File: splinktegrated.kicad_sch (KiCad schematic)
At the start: 126 parts, among them J1 USB_C_Receptacle_USB2.0, J10 NA_Ribbon, J13 Conn_01x01_Socket, J14 Cirque, J15 Conn_01x01_Socket, J16 Conn_01x01_Socket, J17 Conn_01x01_Socket, J18 USB_C_Receptacle_USB2.0, J19 Conn_01x01_Socket, J20 Conn_01x01_Socket, J5 Conn_01x02, J6 Cirque, J7 NA_trackball, J8 NA_Ribbon, J9 NA_RGB, Q4 AO3401A, Q5 AO3401A, SW2 NA_SW_SPST, SW9001 NA_SW_SPST, U1 RP2040, U2 USBLC6-2P6, U3 XC6210B332MR-G, U4 USBLC6-2P6, U5 W25Q128JVS, U6 74LVC1T45, Y1 Crystal_GND24

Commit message: connect stuff
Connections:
- net D+: no longer right_J9001.A6 (D+), right_J9001.B6 (D+), right_R9005.1, right_U9003.3 (I/O2), right_U9003.4 (I/O2)
- net D-: no longer right_J9001.A7 (D-), right_J9001.B7 (D-), right_R9006.1, right_U9003.1 (I/O1), right_U9003.6 (I/O1)
- net GND: no longer SW9001.2 (B), right_C9000.2, right_C9001.2, right_C9002.2, right_C9003.2, right_C9004.2, right_C9005.2, right_C9006.2, right_C9007.2, right_C9008.2, right_C9009.2, right_C9010.2, right_C9011.2, right_C9012.2, right_C9013.2, right_D9000.2 (A2), right_FB9001.1, right_FB9002.1, right_H9001.1, right_H9003.1, right_J9000.A1 (GND), right_J9000.A12 (GND), right_J9000.B1 (GND), right_J9000.B12 (GND), right_J9001.A1 (GND), right_J9001.A12 (GND), right_J9001.B1 (GND), right_J9001.B12 (GND), right_J9004.1 (Pin_1), right_J9006.2 (Pin_2), right_J9008.6 (Pin_6), right_J9014.11 (Pin_11), right_Q9000.1 (G), right_Q9001.1 (G), right_R9000.2, right_R9001.2, right_R9002.1, right_R9010.1, right_R9011.1, right_U9000.2 (GND), right_U9001.2 (GND), right_U9002.2 (GND), right_U9003.2 (GND), right_U9004.4 (GND), right_U9005.19 (TESTEN), right_U9005.57 (GND), right_Y9000.2, right_Y9000.4
- net rgb_5V: no longer right_J9006.3 (Pin_3), right_J9014.8 (Pin_8), right_U9001.4 (B)
- new net right_D+: right_J9001.A6 (D+), right_J9001.B6 (D+), right_R9005.1, right_U9003.3 (I/O2), right_U9003.4 (I/O2)
- new net right_D-: right_J9001.A7 (D-), right_J9001.B7 (D-), right_R9006.1, right_U9003.1 (I/O1), right_U9003.6 (I/O1)
- new net right_GND: SW9001.2 (B), right_C9000.2, right_C9001.2, right_C9002.2, right_C9003.2, right_C9004.2, right_C9005.2, right_C9006.2, right_C9007.2, right_C9008.2, right_C9009.2, right_C9010.2, right_C9011.2, right_C9012.2, right_C9013.2, right_D9000.2 (A2), right_FB9001.1, right_FB9002.1, right_H9001.1, right_H9003.1, right_J9000.A1 (GND), right_J9000.A12 (GND), right_J9000.B1 (GND), right_J9000.B12 (GND), right_J9001.A1 (GND), right_J9001.A12 (GND), right_J9001.B1 (GND), right_J9001.B12 (GND), right_J9004.1 (Pin_1), right_J9006.2 (Pin_2), right_J9008.6 (Pin_6), right_J9014.11 (Pin_11), right_Q9000.1 (G), right_Q9001.1 (G), right_R9000.2, right_R9001.2, right_R9002.1, right_R9010.1, right_R9011.1, right_U9000.2 (GND), right_U9001.2 (GND), right_U9002.2 (GND), right_U9003.2 (GND), right_U9004.4 (GND), right_U9005.19 (TESTEN), right_U9005.57 (GND), right_Y9000.2, right_Y9000.4
- new net right_rgb_5V: right_J9006.3 (Pin_3), right_J9014.8 (Pin_8), right_U9001.4 (B)
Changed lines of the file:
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@@
 		)
 	)
-	(text "Old"
-		(exclude_from_sim no)
-		(at -67.31 384.81 0)
-		(effects
-			(font
-				(size 1.778 1.778)
-				(thickness 0.3556)
-				(bold yes)
-			)
-			(justify left bottom)
-		)
-	)
 	(text "Indicator & buttons"
 		(exclude_from_sim no)
@@
 		)
 	)
-	(wire
-		(pts
-			(xy -53.34 391.16) (xy -44.45 391.16)
-		)
-		(stroke
-			(width 0)
-			(type default)
-		)
-	)
 	(polyline
 		(pts
@@
 	(wire
 		(pts
-			(xy -53.34 388.62) (xy -44.45 388.62)
-		)
-		(stroke
-			(width 0)
-			(type default)
-		)
-	)
-	(wire
-		(pts
 			(xy 287.02 370.84) (xy 275.59 370.84)
 		)
@@
 	(wire
 		(pts
-			(xy -53.34 396.24) (xy -44.45 396.24)
-		)
-		(stroke
-			(width 0)
-			(type default)
-		)
-	)
-	(wire
-		(pts
 			(xy 248.92 370.84) (xy 250.19 370.84)
 		)
@@
 		)
 	)
-	(wire
-		(pts
-			(xy -53.34 393.7) (xy -44.45 393.7)
-		)
-		(stroke
-			(width 0)
-			(type default)
-		)
-	)
 	(polyline
 		(pts
@@
 		)
 	)
-	(label "D-_daughter"
-		(at -53.34 393.7 180)
-		(effects
-			(font
-				(size 1.27 1.27)
-			)
-			(justify right bottom)
-		)
-	)
 	(label "right_SCLK"
 		(at 274.32 300.99 0)
@@
 		)
 	)
-	(label "Vbus_mother"
-		(at -44.45 388.62 0)
-		(effects
-			(font
-				(size 1.27 1.27)
-			)
-			(justify left bottom)
-		)
-	)
-	(label "right_D-"
-		(at -44.45 393.7 0)
-		(effects
-			(font
-				(size 1.27 1.27)
-			)
-			(justify left bottom)
-		)
-	)
 	(label "right_D0"
 		(at 210.82 299.72 180)
@@
 		)
 	)
-	(label "right_D+"
-		(at -44.45 396.24 0)
-		(effects
-			(font
-				(size 1.27 1.27)
-			)
-			(justify left bottom)
-		)
-	)
-	(label "D+_daughter"
-		(at -53.34 396.24 180)
-		(effects
-			(font
-				(size 1.27 1.27)
-			)
-			(justify right bottom)
-		)
-	)
 	(label "right_D14"
 		(at 322.58 335.28 0)
@@
 		)
 	)
-	(label "Vbus_daughter"
-		(at -53.34 388.62 180)
-		(effects
-			(font
-				(size 1.27 1.27)
-			)
-			(justify right bottom)
-		)
-	)
 	(label "right_SCLK"
 		(at 210.82 355.6 180)
@@
 		)
 	)
-	(label "Gnd_daughter"
-		(at -53.34 391.16 180)
-		(effects
-			(font
-				(size 1.27 1.27)
-			)
-			(justify right bottom)
-		)
-	)
 	(label "right_LED"
 		(at 210.82 342.9 180)
@@
 		)
 	)
-	(global_label "rgb_5V"
+	(global_label "right_rgb_5V"
 		(shape input)
 		(at 353.06 273.05 180)
@@
 		)
 	)
-	(global_label "rgb_5V"
+	(global_label "right_rgb_5V"
 		(shape input)
 		(at 450.85 285.75 180)
@@
 		)
 	)
-	(global_label "rgb_5V"
+	(global_label "right_rgb_5V"
 		(shape input)
 		(at 363.22 408.94 0)
@@
 					(unit 1)
 				)
-			)
-		)
-	)
-	(symbol
-		(lib_id "power:GND")
-		(at -44.45 391.16 90)
-		(unit 1)
-		(exclude_from_sim no)
-		(in_bom yes)
-		(on_board yes)
-		(dnp no)
-		(property "Reference" "#PWR058"
-			(at -38.1 391.16 0)
-			(effects
-				(font
-					(size 1.27 1.27)
-				)
-				(hide yes)
-			)
-		)
-		(property "Value" "right_GND"
-			(at -37.4651 391.316 90)
-			(effects
-				(font
-					(size 1.27 1.27)
-				)
-				(justify left)
-			)
-		)
-		(property "Footprint" ""
-			(at -44.45 391.16 0)
-			(effects
-				(font
-					(size 1.27 1.27)
-				)
-				(hide yes)
-			)
-		)
-		(property "Datasheet" ""
-			(at -44.45 391.16 0)
-			(effects
-				(font
-					(size 1.27 1.27)
-				)
-				(hide yes)
-			)
-		)
-		(property "Description" ""
-			(at -44.45 391.16 0)
-			(effects
-				(font
-					(size 1.27 1.27)
-				)
-				(hide yes)
-			)
-		)
-		(pin "1"
-		)
-		(instances
-			(project "splinktegrated"
-				(path "/7353e96a-343a-4876-b497-b1d205a14d97"
-					(reference "#PWR058")
-					(unit 1)
-				)

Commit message: change push button
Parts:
- J5, right_J9004: footprint drawings:PinHeader_1x02_P1.27mm_Vertical -> Button_Switch_SMD:SW_SPST_CK_KXT3
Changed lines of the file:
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@@
 			)
 		)
-		(property "Footprint" "drawings:PinHeader_1x02_P1.27mm_Vertical"
+		(property "Footprint" "Button_Switch_SMD:SW_SPST_CK_KXT3"
 			(at 69.215 174.625 0)
 			(effects
@@
 			)
 		)
-		(property "Footprint" "drawings:PinHeader_1x02_P1.27mm_Vertical"
+		(property "Footprint" "Button_Switch_SMD:SW_SPST_CK_KXT3"
 			(at 88.265 415.925 0)
 			(effects

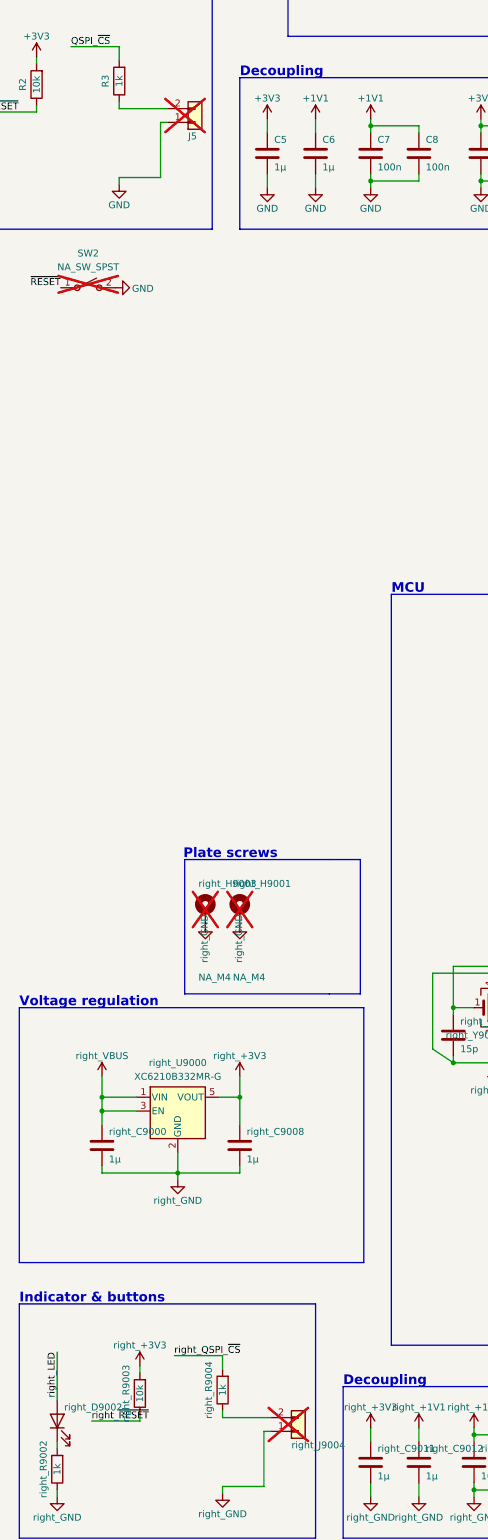
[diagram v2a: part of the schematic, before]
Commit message: populate hardware fallback button
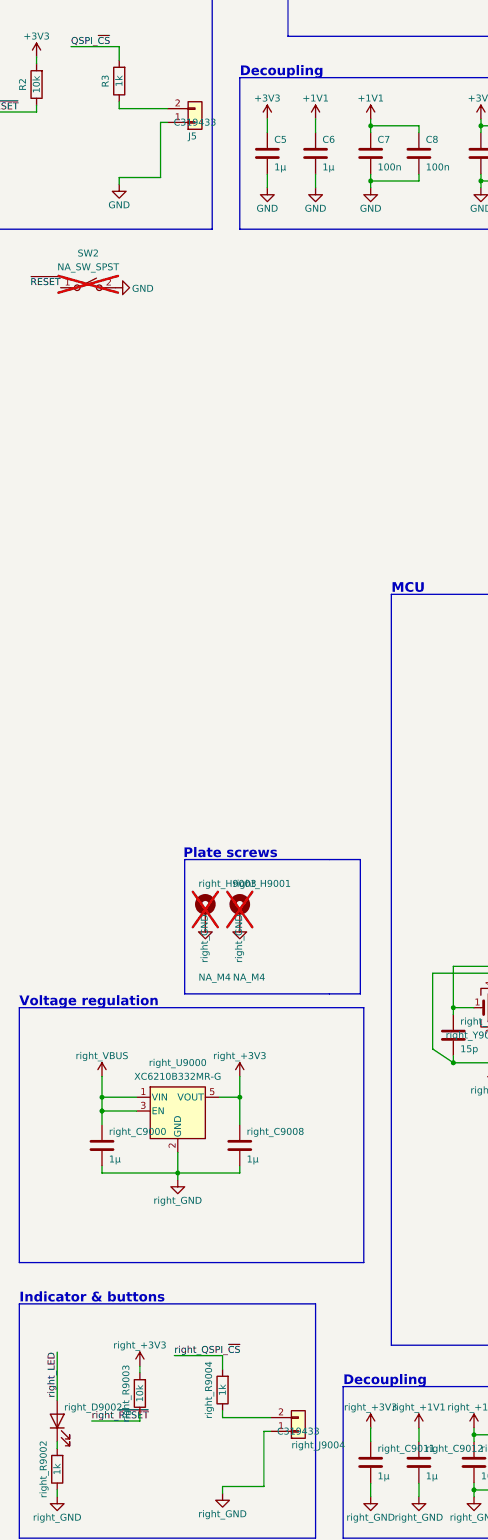
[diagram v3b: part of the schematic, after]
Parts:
- J5, right_J9004: LCSC (none) -> C319433; now fitted; now in the parts list
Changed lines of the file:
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@@
 		(unit 1)
 		(exclude_from_sim no)
-		(in_bom no)
+		(in_bom yes)
 		(on_board yes)
-		(dnp yes)
+		(dnp no)
 		(property "Reference" "J5"
 			(at 67.945 177.165 0)
@@
 			)
 		)
+		(property "LCSC" "C319433"
+			(at 69.215 174.625 0)
+			(effects
+				(font
+					(size 1.27 1.27)
+				)
+			)
+		)
 		(pin "1"
 		)
@@
 		(unit 1)
 		(exclude_from_sim no)
-		(in_bom no)
+		(in_bom yes)
 		(on_board yes)
-		(dnp yes)
+		(dnp no)
 		(property "Reference" "right_J9004"
 			(at 86.995 418.465 0)
@@
 			)
 		)
+		(property "LCSC" "C319433"
+			(at 88.265 415.925 0)
+			(effects
+				(font
+					(size 1.27 1.27)
+				)
+			)
+		)

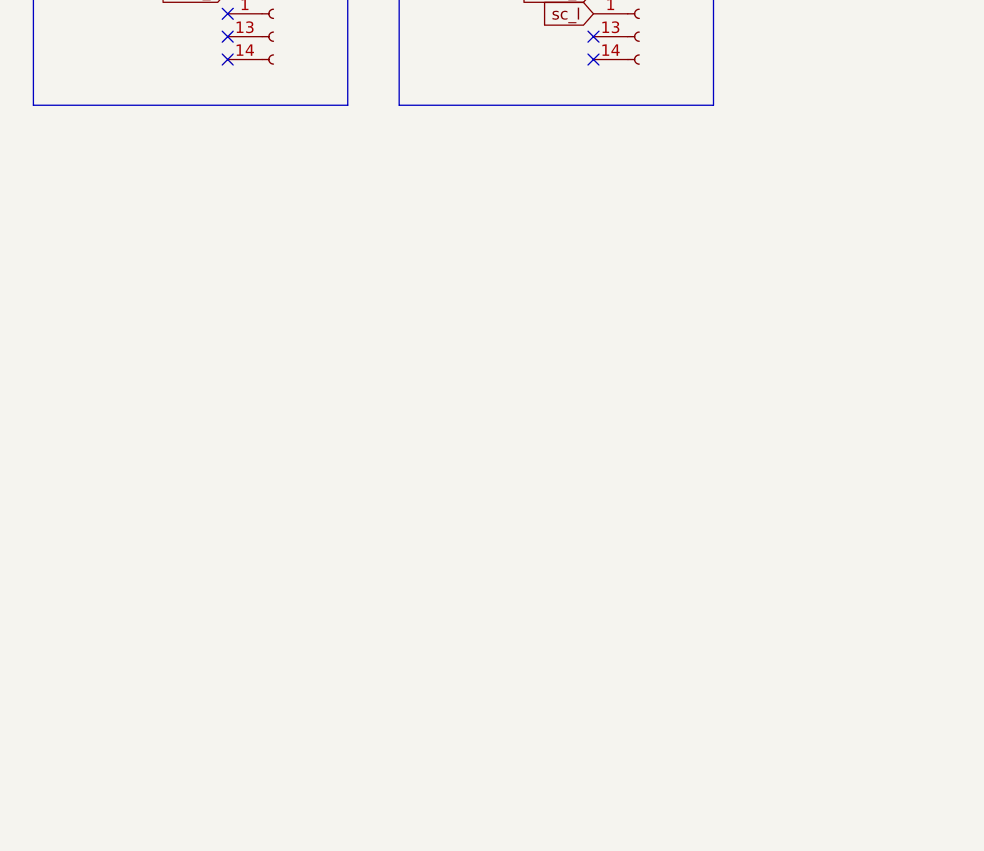
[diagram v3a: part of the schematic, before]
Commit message: add tvs diodes... so many of them
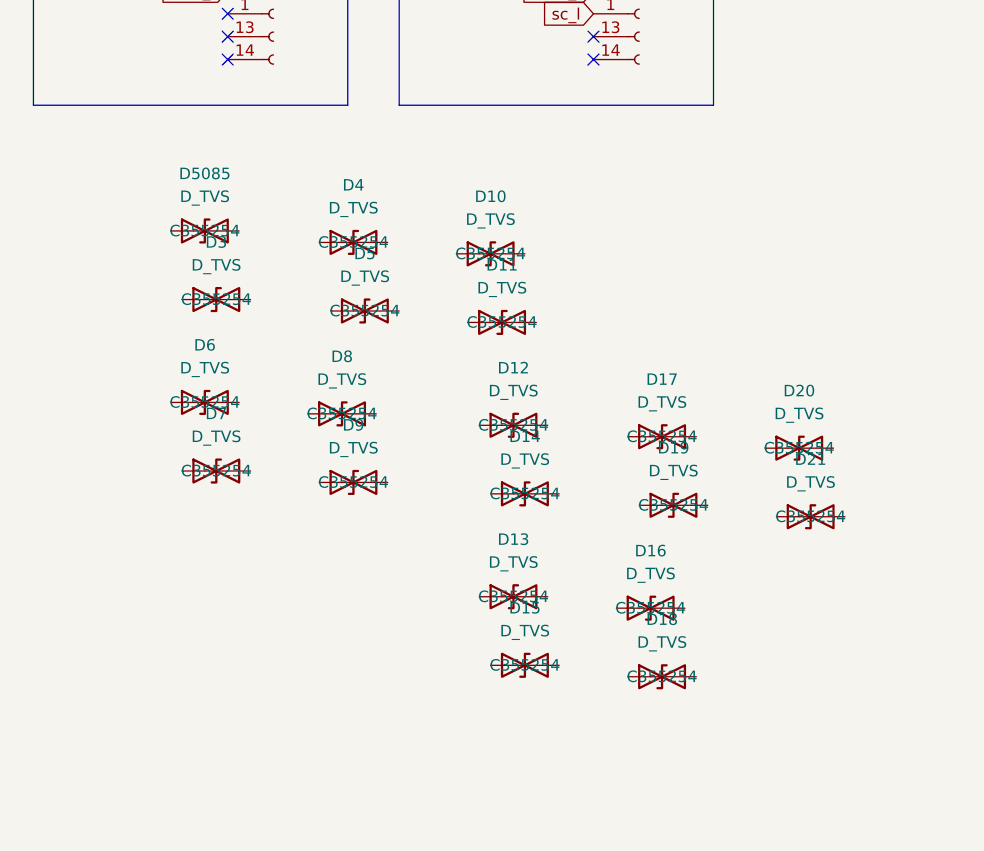
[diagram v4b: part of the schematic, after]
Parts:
- added D10, D11, D12, D13, D14, D15, D16, D17, D18, D19, D20, D21, D3, D4, D5, D5085, D6, D7, D8, D9: D_TVS, Diode_SMD:D_SOD-523, symbol Device:D_TVS

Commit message: routing
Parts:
- removed J6, right_J9014: Cirque, local-libraries:FPC-SMD_FPC05012-09200-.5mm, symbol Connector:Conn_01x14_Female
- removed NA_JP5, right_NA_JP9000: NA_Jumper_2_Open, local-libraries:SolderJumper-2_P1.3mm_Open_TrianglePad1.0x1.5mm, symbol Jumper:Jumper_2_Open
- added D22, D23, D24, D25, D28, D29, D30, D31, D32, D33, D34, D35, D36, D37, D38, D40, D41, D42: D_TVS, Diode_SMD:D_SOD-523, symbol Device:D_TVS
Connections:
- net right_D13: now also D31.2 (A2)
- net right_D14: now also D30.2 (A2)
- net right_GND: now also D22.1 (A1), D23.1 (A1), D24.1 (A1), D25.1 (A1), D28.1 (A1), D29.1 (A1), D30.1 (A1), D31.1 (A1), D32.2 (A2), D33.2 (A2), D34.2 (A2), D35.2 (A2), D36.2 (A2), D37.2 (A2), D38.2 (A2), D40.2 (A2), D41.2 (A2), D42.2 (A2)
- net right_MISO_l: now also D23.2 (A2)
- net right_MOSI_l: now also D29.2 (A2)
- net right_col1_l: now also D38.1 (A1)
- net right_col2_l: now also D42.1 (A1)
- net right_col3_l: now also D35.1 (A1)
- net right_col4_l: now also D32.1 (A1)
- net right_col6_l: now also D40.1 (A1)
- net right_rgb_3v3: now also D28.2 (A2)
- net right_right_col5_l: now also D37.1 (A1)
- net right_row1_l: now also D22.2 (A2)
- net right_row2_l: now also D36.1 (A1)
- net right_row3_l: now also D34.1 (A1)
- net right_row4_l: now also D33.1 (A1)
- net right_row5_l: now also D41.1 (A1)
- net right_sc_l: now also D24.2 (A2)
- net right_ss_l: now also D25.2 (A2)
- no-connect marks 32 -> 28
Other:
- note removed: "Trackball FPC Connector"
